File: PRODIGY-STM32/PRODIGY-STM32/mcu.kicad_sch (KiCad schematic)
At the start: 21 parts, among them U2 STM32U5F9ZJTxQ

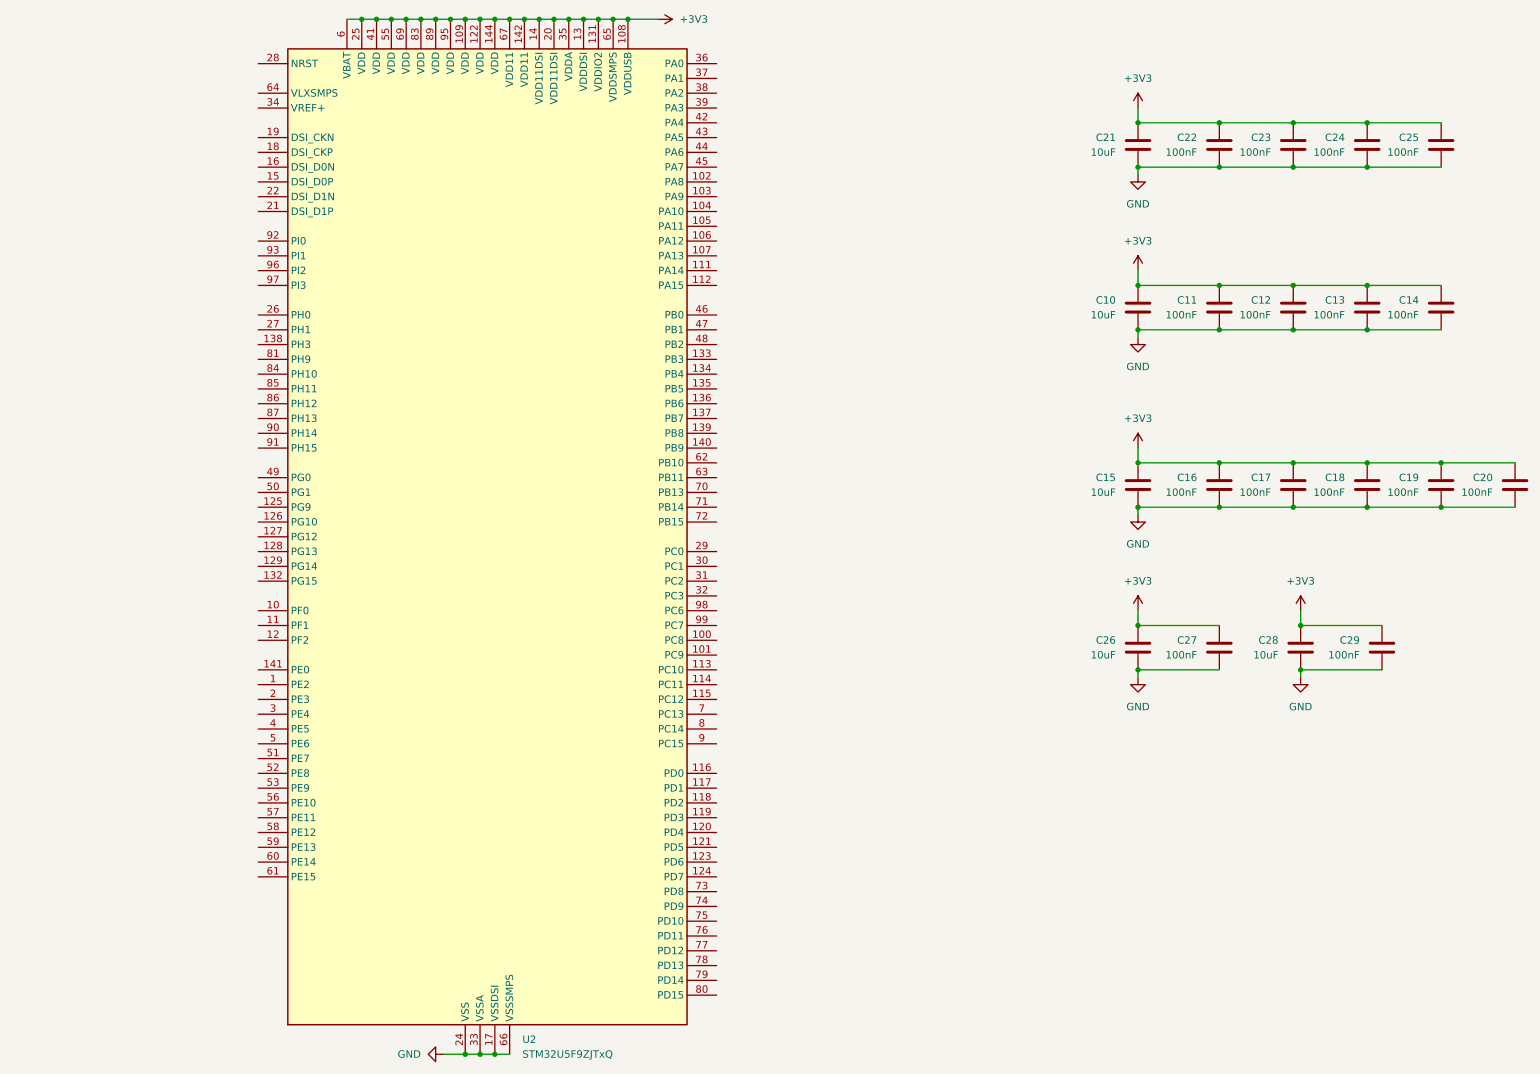
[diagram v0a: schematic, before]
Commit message: stm32 schematic finished
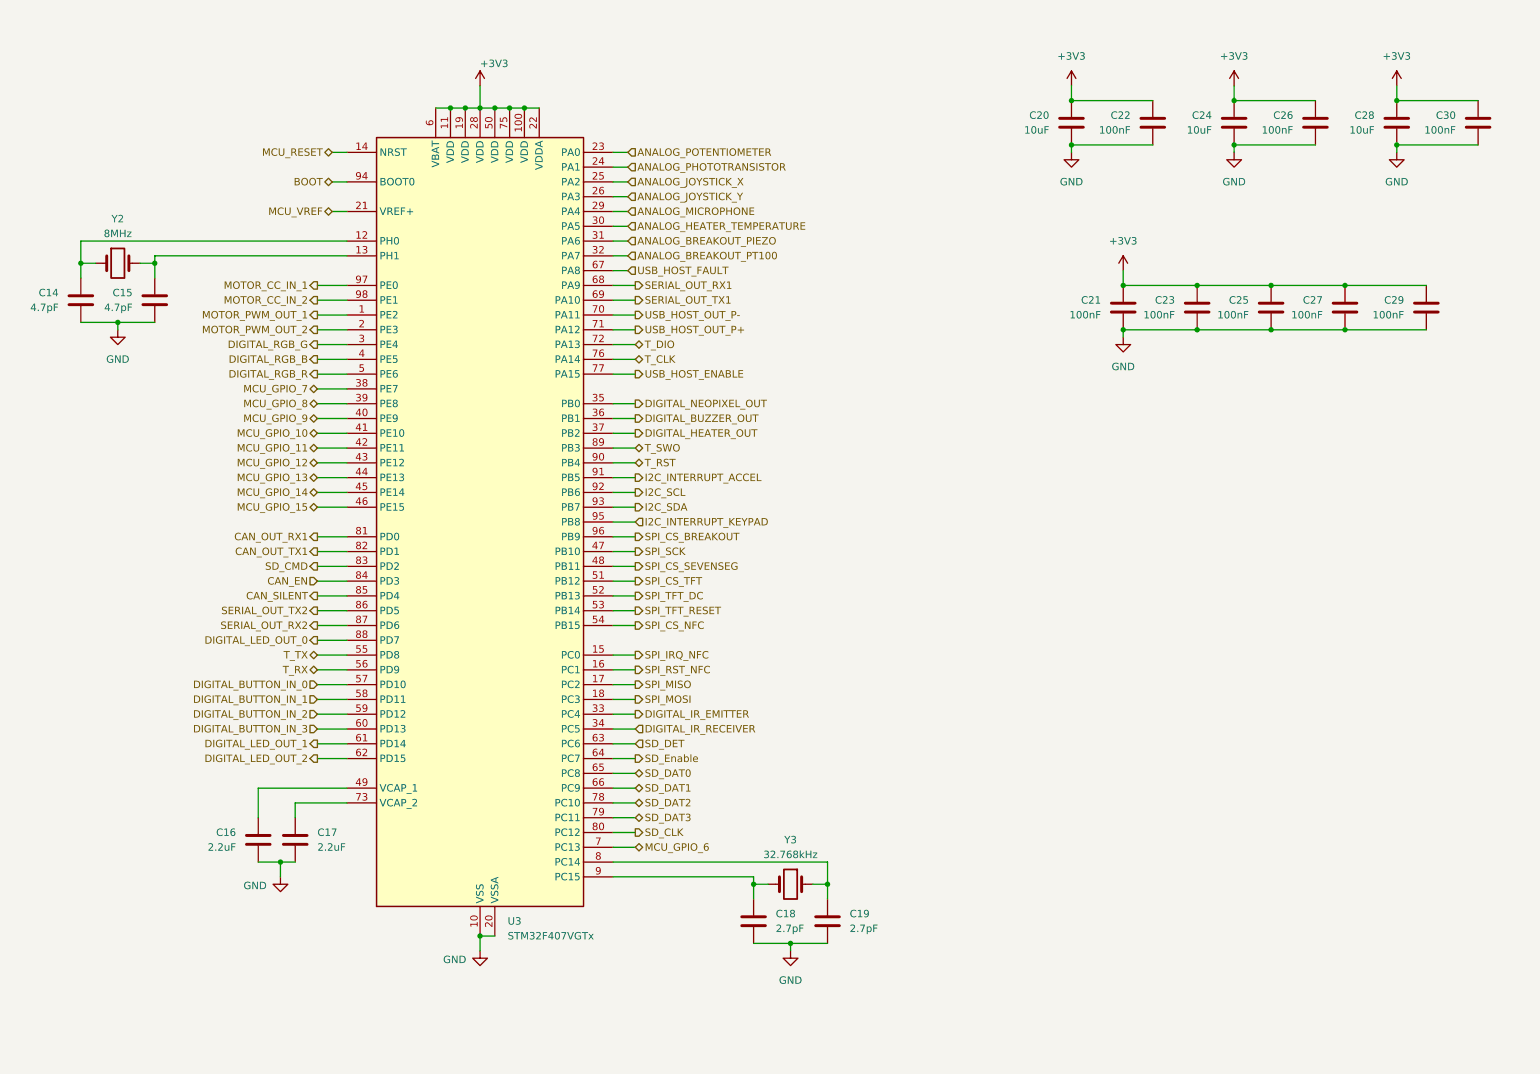
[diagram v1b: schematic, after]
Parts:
- removed C10: 10uF, symbol Device:C
- removed C11, C12, C13, C20, C24: 100nF, symbol Device:C
- removed U2: STM32U5F9ZJTxQ, Package_QFP:LQFP-144_20x20mm_P0.5mm, symbol MCU_ST_STM32U5:STM32U5F9ZJTxQ
- added C15: 4.7pF, symbol Device:C
- added C27, C29: 100nF, symbol Device:C
- added U3: STM32F407VGTx, Package_QFP:LQFP-100_14x14mm_P0.5mm, symbol MCU_ST_STM32F4:STM32F407VGTx
- added Y2: 8MHz, symbol Device:Crystal
- added Y3: 32.768kHz, symbol Device:Crystal
- C14: value 100nF -> 4.7pF
- C16, C17: value 100nF -> 2.2uF
- C18, C19: value 100nF -> 2.7pF
- C21: value 10uF -> 100nF
- renumbered C15 to C20, C26 to C24, C27 to C26, C29 to C30
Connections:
- net +3V3: now also C27.1, C29.1, U3.100 (VDD), U3.11 (VDD), U3.19 (VDD), U3.22 (VDDA), U3.28 (VDD), U3.50 (VDD), U3.6 (VBAT), U3.75 (VDD); no longer C14.1, C16.1, C17.1, C18.1, C19.1
- net GND: now also C15.2, C27.2, C29.2, U3.10 (VSS), U3.20 (VSSA), U3.27 (VSS), U3.74 (VSS), U3.99 (VSS)
- new net: C14.1, U3.12 (PH0), Y2.1
- new net: C16.1, U3.49 (VCAP_1)
- new net: C15.1, U3.13 (PH1), Y2.2
- new net: C17.1, U3.73 (VCAP_2)
- new net: C19.1, U3.8 (PC14), Y3.1
- new net: C18.1, U3.9 (PC15), Y3.2
- new net ANALOG_BREAKOUT_PIEZO: U3.31 (PA6)
- new net ANALOG_BREAKOUT_PT100: U3.32 (PA7)
- new net ANALOG_HEATER_TEMPERATURE: U3.30 (PA5)
- new net ANALOG_JOYSTICK_X: U3.25 (PA2)
- new net ANALOG_JOYSTICK_Y: U3.26 (PA3)
- new net ANALOG_MICROPHONE: U3.29 (PA4)
- new net ANALOG_PHOTOTRANSISTOR: U3.24 (PA1)
- new net ANALOG_POTENTIOMETER: U3.23 (PA0)
- new net BOOT: U3.94 (BOOT0)
- new net CAN_EN: U3.84 (PD3)
- new net CAN_OUT_RX1: U3.81 (PD0)
- new net CAN_OUT_TX1: U3.82 (PD1)
- new net CAN_SILENT: U3.85 (PD4)
- new net DIGITAL_BUTTON_IN_0: U3.57 (PD10)
- new net DIGITAL_BUTTON_IN_1: U3.58 (PD11)
- new net DIGITAL_BUTTON_IN_2: U3.59 (PD12)
- new net DIGITAL_BUTTON_IN_3: U3.60 (PD13)
- new net DIGITAL_BUZZER_OUT: U3.36 (PB1)
- new net DIGITAL_HEATER_OUT: U3.37 (PB2)
- new net DIGITAL_IR_EMITTER: U3.33 (PC4)
- new net DIGITAL_IR_RECEIVER: U3.34 (PC5)
- new net DIGITAL_LED_OUT_0: U3.88 (PD7)
- new net DIGITAL_LED_OUT_1: U3.61 (PD14)
- new net DIGITAL_LED_OUT_2: U3.62 (PD15)
- new net DIGITAL_NEOPIXEL_OUT: U3.35 (PB0)
- new net DIGITAL_RGB_B: U3.4 (PE5)
- new net DIGITAL_RGB_G: U3.3 (PE4)
- new net DIGITAL_RGB_R: U3.5 (PE6)
- new net I2C_INTERRUPT_ACCEL: U3.91 (PB5)
- new net I2C_INTERRUPT_KEYPAD: U3.95 (PB8)
- new net I2C_SCL: U3.92 (PB6)
- new net I2C_SDA: U3.93 (PB7)
- new net MCU_GPIO_10: U3.41 (PE10)
- new net MCU_GPIO_11: U3.42 (PE11)
- new net MCU_GPIO_12: U3.43 (PE12)
- new net MCU_GPIO_13: U3.44 (PE13)
- new net MCU_GPIO_14: U3.45 (PE14)
- new net MCU_GPIO_15: U3.46 (PE15)
- new net MCU_GPIO_6: U3.7 (PC13)
- new net MCU_GPIO_7: U3.38 (PE7)
- new net MCU_GPIO_8: U3.39 (PE8)
- new net MCU_GPIO_9: U3.40 (PE9)
- new net MCU_RESET: U3.14 (NRST)
- new net MCU_VREF: U3.21 (VREF+)
- new net MOTOR_CC_IN_1: U3.97 (PE0)
- new net MOTOR_CC_IN_2: U3.98 (PE1)
- new net MOTOR_PWM_OUT_1: U3.1 (PE2)
- new net MOTOR_PWM_OUT_2: U3.2 (PE3)
- new net SD_CLK: U3.80 (PC12)
- new net SD_CMD: U3.83 (PD2)
- new net SD_DAT0: U3.65 (PC8)
- new net SD_DAT1: U3.66 (PC9)
- new net SD_DAT2: U3.78 (PC10)
- new net SD_DAT3: U3.79 (PC11)
- new net SD_DET: U3.63 (PC6)
- new net SD_Enable: U3.64 (PC7)
- new net SERIAL_OUT_RX1: U3.68 (PA9)
- new net SERIAL_OUT_RX2: U3.87 (PD6)
- new net SERIAL_OUT_TX1: U3.69 (PA10)
- new net SERIAL_OUT_TX2: U3.86 (PD5)
- new net SPI_CS_BREAKOUT: U3.96 (PB9)
- new net SPI_CS_NFC: U3.54 (PB15)
- new net SPI_CS_SEVENSEG: U3.48 (PB11)
- new net SPI_CS_TFT: U3.51 (PB12)
- new net SPI_IRQ_NFC: U3.15 (PC0)
- new net SPI_MISO: U3.17 (PC2)
- new net SPI_MOSI: U3.18 (PC3)
- new net SPI_RST_NFC: U3.16 (PC1)
- new net SPI_SCK: U3.47 (PB10)
- new net SPI_TFT_DC: U3.52 (PB13)
- new net SPI_TFT_RESET: U3.53 (PB14)
- new net T_CLK: U3.76 (PA14)
- new net T_DIO: U3.72 (PA13)
- new net T_RST: U3.90 (PB4)
- new net T_RX: U3.56 (PD9)
- new net T_SWO: U3.89 (PB3)
- new net T_TX: U3.55 (PD8)
- new net USB_HOST_ENABLE: U3.77 (PA15)
- new net USB_HOST_FAULT: U3.67 (PA8)
- new net USB_HOST_OUT_P+: U3.71 (PA12)
- new net USB_HOST_OUT_P-: U3.70 (PA11)
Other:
- moved on the sheet: C20, C24, C26, C28, C30

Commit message: All footprint assosiations have been made across all schematics.
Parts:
- C14, C15, C18, C19, C21, C22, C23, C25, C26, C27, C29, C30: footprint (none) -> Capacitor_SMD:C_0603_1608Metric
- C16, C17, C20, C24, C28: footprint (none) -> Capacitor_SMD:C_0805_2012Metric
- Y2, Y3: footprint (none) -> Crystal:Crystal_SMD_3225-4Pin_3.2x2.5mm
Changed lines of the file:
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@@
 			)
 		)
-		(property "Footprint" ""
+		(property "Footprint" "Capacitor_SMD:C_0603_1608Metric"
 			(at 32.0548 68.58 0)
 			(effects
@@
 			)
 		)
-		(property "Footprint" ""
+		(property "Footprint" "Capacitor_SMD:C_0805_2012Metric"
 			(at 64.4652 161.29 0)
 			(effects
@@
 			)
 		)
-		(property "Footprint" ""
+		(property "Footprint" "Capacitor_SMD:C_0805_2012Metric"
 			(at 202.2348 38.1 0)
 			(effects
@@
 			)
 		)
-		(property "Footprint" ""
+		(property "Footprint" "Crystal:Crystal_SMD_3225-4Pin_3.2x2.5mm"
 			(at 39.37 58.42 0)
 			(effects
@@
 			)
 		)
-		(property "Footprint" ""
+		(property "Footprint" "Capacitor_SMD:C_0805_2012Metric"
 			(at 230.1748 38.1 0)
 			(effects
@@
 			)
 		)
-		(property "Footprint" ""
+		(property "Footprint" "Capacitor_SMD:C_0603_1608Metric"
 			(at 236.5248 69.85 0)
 			(effects
@@
 			)
 		)
-		(property "Footprint" ""
+		(property "Footprint" "Capacitor_SMD:C_0603_1608Metric"
 			(at 249.2248 69.85 0)
 			(effects
@@
 			)
 		)
-		(property "Footprint" ""
+		(property "Footprint" "Capacitor_SMD:C_0603_1608Metric"
 			(at 244.1448 38.1 0)
 			(effects
@@
 			)
 		)
-		(property "Footprint" ""
+		(property "Footprint" "Capacitor_SMD:C_0603_1608Metric"
 			(at 223.8248 69.85 0)
 			(effects
@@
 			)
 		)
-		(property "Footprint" ""
+		(property "Footprint" "Capacitor_SMD:C_0805_2012Metric"
 			(at 258.1148 38.1 0)
 			(effects
@@
 			)
 		)
-		(property "Footprint" ""
+		(property "Footprint" "Crystal:Crystal_SMD_3225-4Pin_3.2x2.5mm"
 			(at 154.94 165.1 0)
 			(effects
@@
 			)
 		)
-		(property "Footprint" ""
+		(property "Footprint" "Capacitor_SMD:C_0805_2012Metric"
 			(at 68.8848 161.29 0)
 			(effects
@@
 			)
 		)
-		(property "Footprint" ""
+		(property "Footprint" "Capacitor_SMD:C_0603_1608Metric"
 			(at 216.2048 38.1 0)
 			(effects
@@
 			)
 		)
-		(property "Footprint" ""
+		(property "Footprint" "Capacitor_SMD:C_0603_1608Metric"
 			(at 162.2552 175.26 0)
 			(effects
@@
 			)
 		)
-		(property "Footprint" ""
+		(property "Footprint" "Capacitor_SMD:C_0603_1608Metric"
 			(at 272.0848 38.1 0)
 			(effects
@@
 			)
 		)
-		(property "Footprint" ""
+		(property "Footprint" "Capacitor_SMD:C_0603_1608Metric"
 			(at 263.1948 69.85 0)
 			(effects
@@
 			)
 		)
-		(property "Footprint" ""
+		(property "Footprint" "Capacitor_SMD:C_0603_1608Metric"
 			(at 44.7548 68.58 0)
 			(effects
@@
 			)
 		)
-		(property "Footprint" ""
+		(property "Footprint" "Capacitor_SMD:C_0603_1608Metric"
 			(at 211.1248 69.85 0)
 			(effects
@@
 			)
 		)
-		(property "Footprint" ""
+		(property "Footprint" "Capacitor_SMD:C_0603_1608Metric"
 			(at 149.5552 175.26 0)
 			(effects

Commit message: STM32 bom done.
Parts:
- C14, C15: TME (none) -> CC0603BRNPO9BN4R7
- C16, C17: TME (none) -> CL21B225KOFNNNE
- C18, C19: TME (none) -> 0603N2R7C500CT
- C20, C24, C28: TME (none) -> CL21A106KOQNNNE
- C21, C22, C23, C25, C26, C27, C29, C30: TME (none) -> CL10B104KB8NNNC
- U3: TME (none) -> STM32F407VGT6
- Y2: footprint Crystal:Crystal_SMD_3225-4Pin_3.2x2.5mm -> Crystal:Crystal_SMD_5032-4Pin_5.0x3.2mm; TME (none) -> 8.00M-CFPX104
- Y3: footprint Crystal:Crystal_SMD_3225-4Pin_3.2x2.5mm -> Crystal:Crystal_SMD_MicroCrystal_CC7V-T1A-2Pin_3.2x1.5mm; TME (none) -> 32.768K-CFPX217

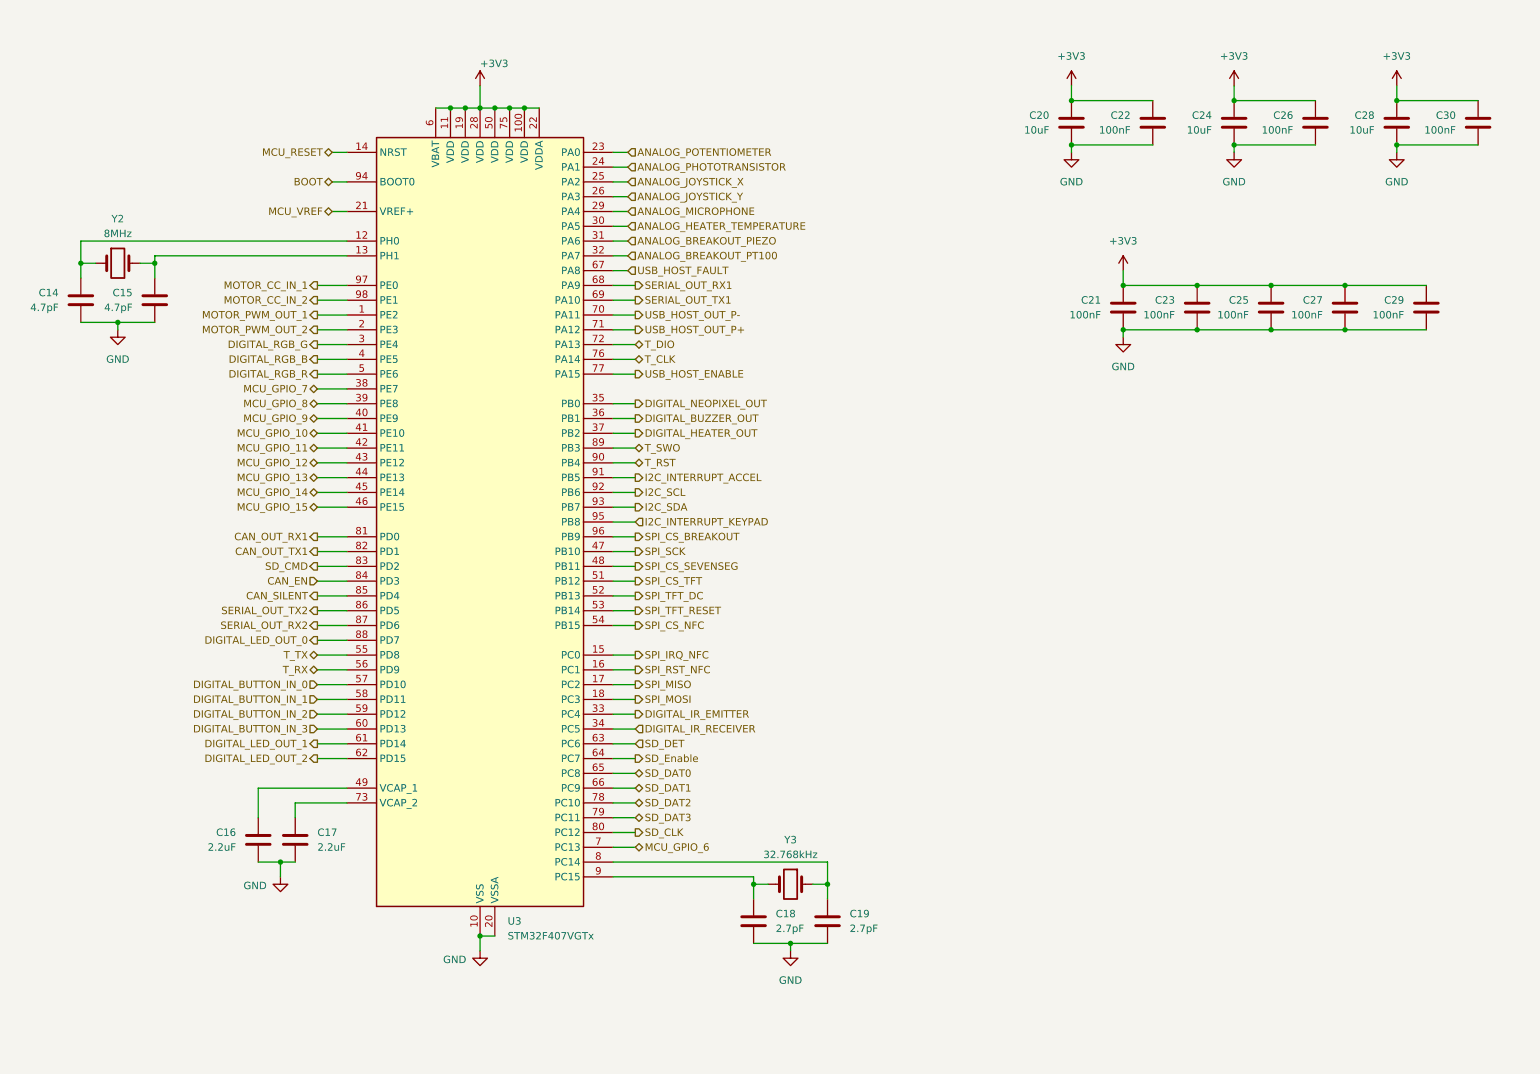
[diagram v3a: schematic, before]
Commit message: ESP32 and ATMEGA bom done.
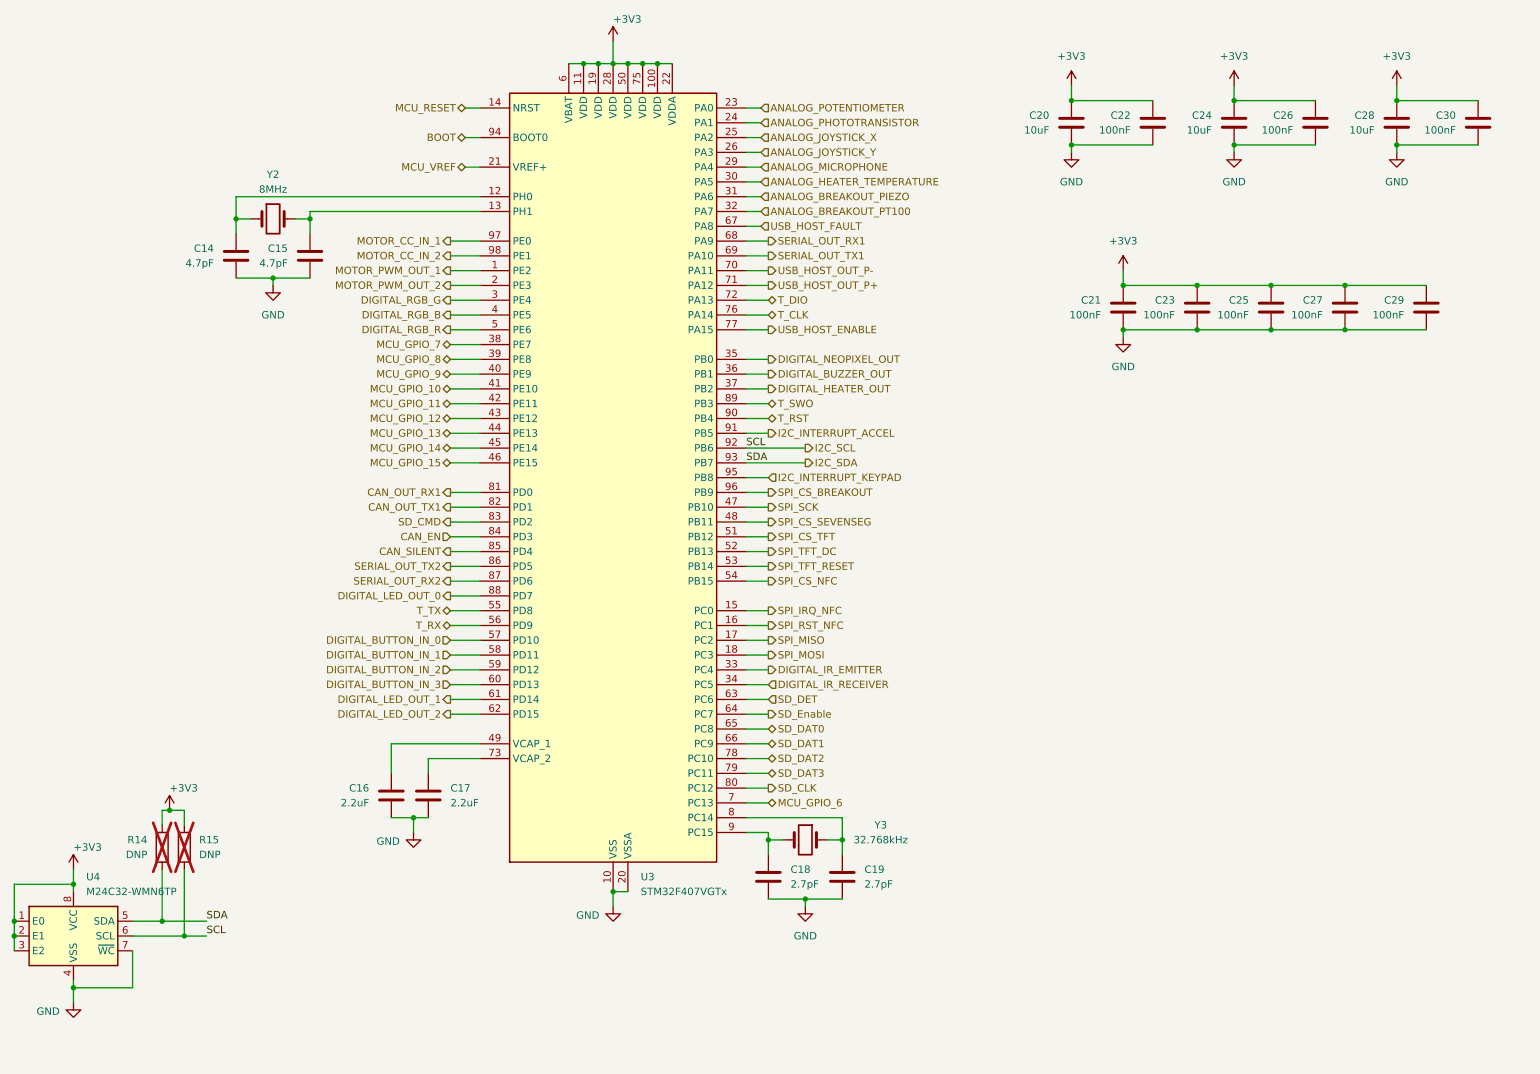
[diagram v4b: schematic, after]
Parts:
- added R14, R15: DNP, Resistor_SMD:R_0603_1608Metric, symbol Device:R
- added U4: M24C32-WMN6TP, Package_SO:SOIC-8_3.9x4.9mm_P1.27mm, symbol Memory_EEPROM:M24C01-FMN
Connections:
- net +3V3: now also R14.1, R15.1, U4.1 (E0), U4.2 (E1), U4.3 (E2), U4.8 (VCC)
- net GND: now also U4.4 (VSS), U4.7 (~{WC})
- net I2C_SCL: now also R15.2, U4.6 (SCL)
- net I2C_SDA: now also R14.2, U4.5 (SDA)
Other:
- moved on the sheet: C14, C15, C16, C17, C18, C19, U3, Y2, Y3
